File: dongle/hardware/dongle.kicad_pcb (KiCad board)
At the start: 2 copper layers, 30 x 50 mm, 45 parts, among them P1 USB, P2 SWD, P3 SMA, SW1 RESET, U1 NCP1117ST33T3G, U2 STM32F072C8Tx, U3 CC2520, Y1 32MHz

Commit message: Final version of PCB, Gerber files.
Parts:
- moved U1 0.40 mm to (87.4, 106.3)
- moved C2 0.30 mm to (89.0, 101.1)
- moved C1 0.30 mm to (88.6, 99.5)
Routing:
- net GND: track 223.7 -> 237.1 mm, vias 64 -> 62
- net Net-(JP1-Pad1): track 3.95 -> 11.0 mm
- net +5V: track 14.3 -> 15.0 mm
- added copper zone on B.Cu, net Net-(JP1-Pad1)

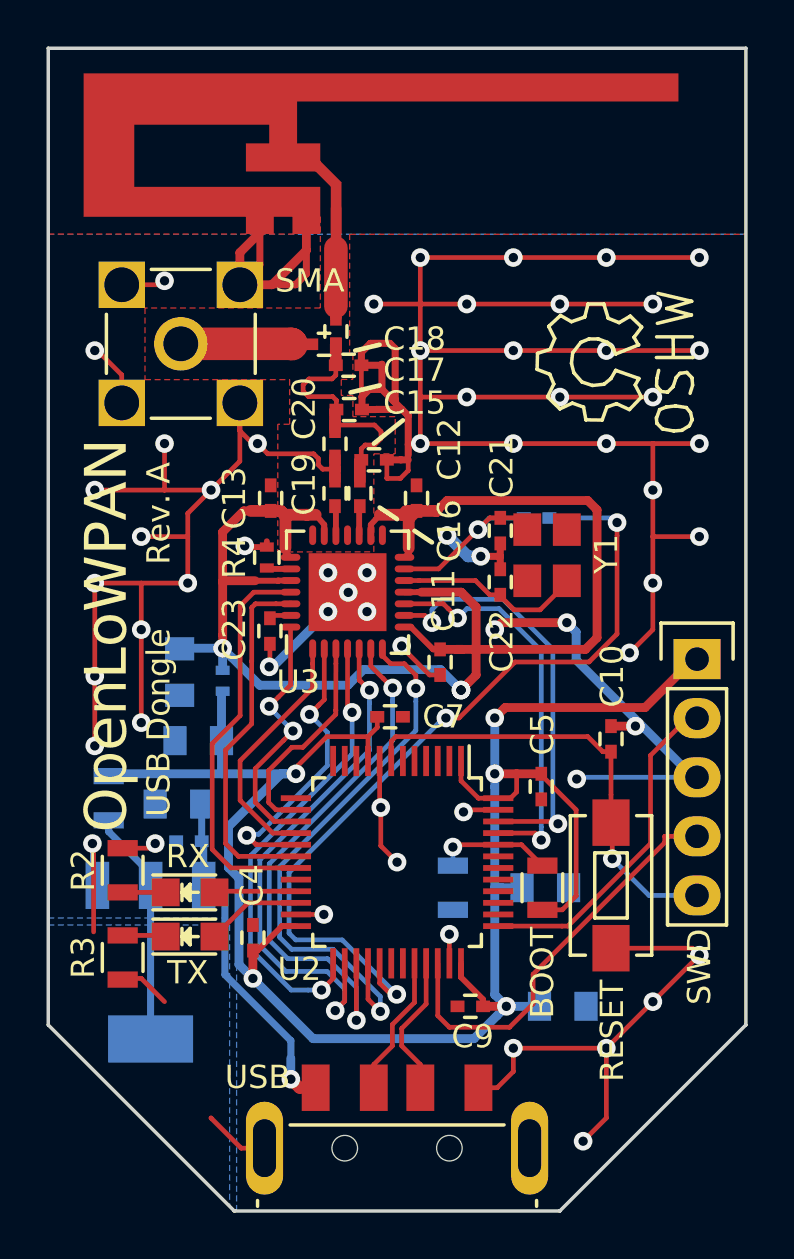
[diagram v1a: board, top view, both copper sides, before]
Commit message: Fix USB connector flipped.
Update schematic to new kicad.
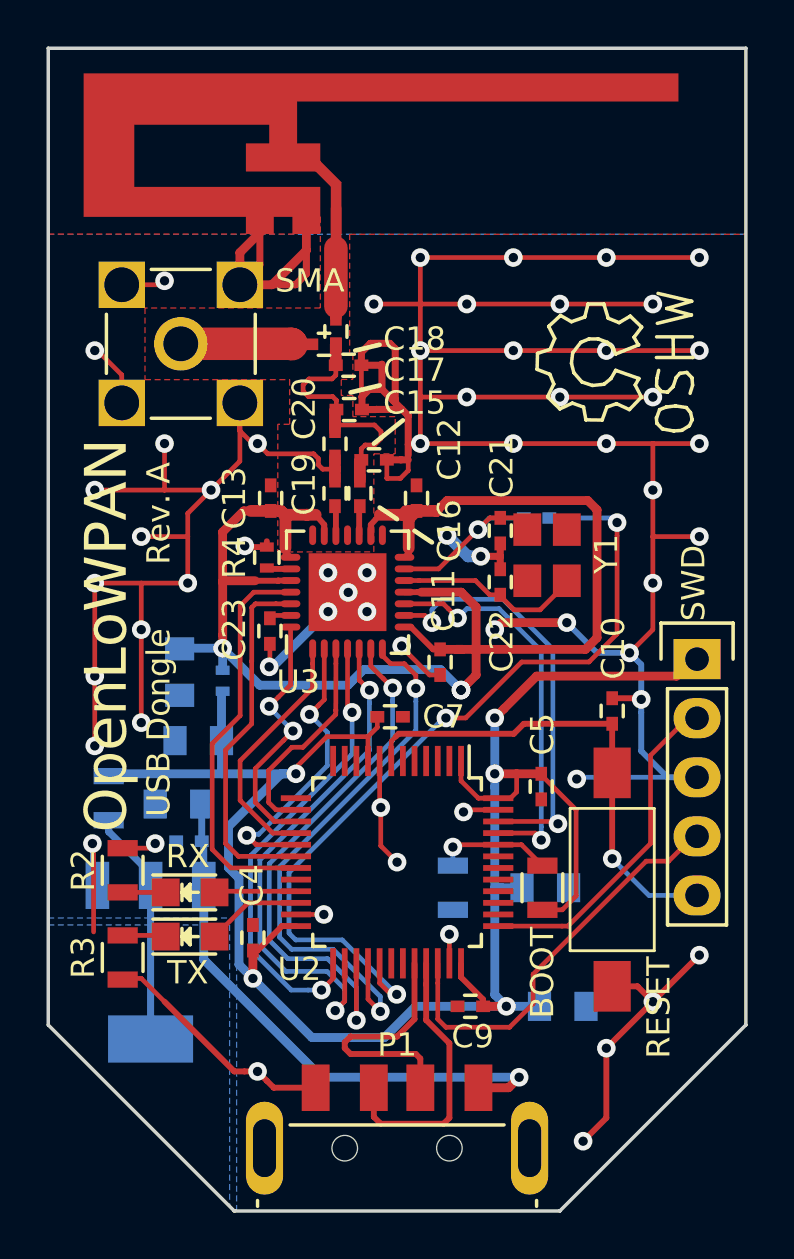
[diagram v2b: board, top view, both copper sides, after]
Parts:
- removed SW1: RESET, Buttons_Switches_SMD:SW_SPST_EVQPE1
- added RESET: RESET, Buttons_Switches_SMD:SW_SPST_FSMSM, F.Cu at (107.2, 102.8)
- moved C10 1.20 mm to (107.2, 95.5)
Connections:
- U2 pad 10: Net-(U2-Pad10) -> (no net)
- U2 pad 11: Net-(U2-Pad11) -> (no net)
- U2 pad 12: Net-(U2-Pad12) -> (no net)
- U2 pad 13: Net-(U2-Pad13) -> (no net)
- U2 pad 2: Net-(U2-Pad2) -> (no net)
- U2 pad 20: Net-(U2-Pad20) -> (no net)
- U2 pad 3: Net-(U2-Pad3) -> (no net)
- U2 pad 30: Net-(U2-Pad30) -> (no net)
- U2 pad 31: Net-(U2-Pad31) -> (no net)
- U2 pad 38: Net-(U2-Pad38) -> (no net)
- U2 pad 39: Net-(U2-Pad39) -> (no net)
- U2 pad 4: Net-(U2-Pad4) -> (no net)
- U2 pad 40: Net-(U2-Pad40) -> (no net)
- U2 pad 41: Net-(U2-Pad41) -> (no net)
- U2 pad 42: Net-(U2-Pad42) -> (no net)
- U2 pad 43: Net-(U2-Pad43) -> (no net)
- U2 pad 5: Net-(U2-Pad5) -> (no net)
- U2 pad 6: Net-(U2-Pad6) -> (no net)
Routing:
- net +5V: track 15.0 -> 24.7 mm
- net /STM32 Microcontroller & Power/D+: track 6.12 -> 11.8 mm
- net /STM32 Microcontroller & Power/D-: track 6.07 -> 10.8 mm
- net /STM32 Microcontroller & Power/~RESET: track 19.7 -> 23.1 mm
- net GND: track 237.1 -> 235.6 mm
